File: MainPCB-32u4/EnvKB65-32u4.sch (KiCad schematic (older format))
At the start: 174 parts, among them U1 ATmega32U4-MU, X1 7050 8MHz 5V

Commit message: changed my mind, I wanted the 32u version to have more switches, going to figure out if I can fit the MCU somewhere on the back of the board.
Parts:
- removed C2: 15pf 0402, Capacitor_SMD:C_0402_1005Metric, symbol Device:C
- removed C7: 0.1uF 0402, Capacitor_SMD:C_0402_1005Metric, symbol Device:C
- removed X1: 7050 8MHz 5V, Oscillator:Oscillator_SMD_SeikoEpson_SG8002CA-4Pin_7.0x5.0mm, symbol Oscillator:SG-7050CAN
- added C2, C7: 20pF 0402, Capacitor_SMD:C_0402_1005Metric, symbol Device:C_Small
- added D_131, D_132, D_271, D_272: Diode SOD-323, Diode_SMD:D_SOD-323_HandSoldering, symbol Device:D_Small
- added K_131, K_132, K_271, K_272: KEYSW, MX_Only:MXOnly-1U-NoLED, symbol MX_Alps_Hybrid:MX-NoLED
- added Y1: 8MHz 5032_2P, Crystal:Crystal_SMD_5032-2Pin_5.0x3.2mm, symbol Device:Crystal
- H0, H1, H2, H3, H4, H5: symbol Mechanical:MountingHole -> Mechanical:MountingHole_Pad
- e1: footprint HRO-TYPE-C31-M-12:HRO-TYPE-C-31-M-12 -> HRO-TYPE-C31-M-12:HRO-TYPE-C-31-M-12-Assembly
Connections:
- net GND: now also H0.1, H1.1, H2.1, H3.1, H4.1, H5.1, C2.1, C7.1
- net XTAL1: now also C2.2, Y1.1
- net XTAL2: now also C7.2, Y1.2
- net col0: no longer U1.10 (PB2)
- net col1: no longer U1.11 (PB3)
- net col10: no longer U1.41 (PF0)
- net col11: no longer U1.1 (PE6)
- net col12: no longer U1.8 (PB0)
- net col13: no longer U1.9 (PB1)
- net col14: no longer U1.20 (PD2)
- net col15: now also K_131.1 (COL), K_271.1 (COL); no longer U1.21 (PD3)
- net col16: now also K_132.1 (COL), K_272.1 (COL); no longer U1.22 (PD5)
- net col2: no longer U1.12 (PB7)
- net col3: no longer U1.18 (PD0)
- net col4: no longer U1.19 (PD1)
- net col5: no longer U1.36 (PF7)
- net col6: no longer U1.37 (PF6)
- net col7: no longer U1.38 (PF5)
- net col8: no longer U1.39 (PF4)
- net col9: no longer U1.40 (PF1)
- net row0: now also D_131.1 (K), D_132.1 (K)
- net row1: now also D_271.1 (K), D_272.1 (K)
- new net: D_272.2 (A), K_272.2 (ROW)
- new net: D_271.2 (A), K_271.2 (ROW)
- new net: D_131.2 (A), K_131.2 (ROW)
- new net: D_132.2 (A), K_132.2 (ROW)

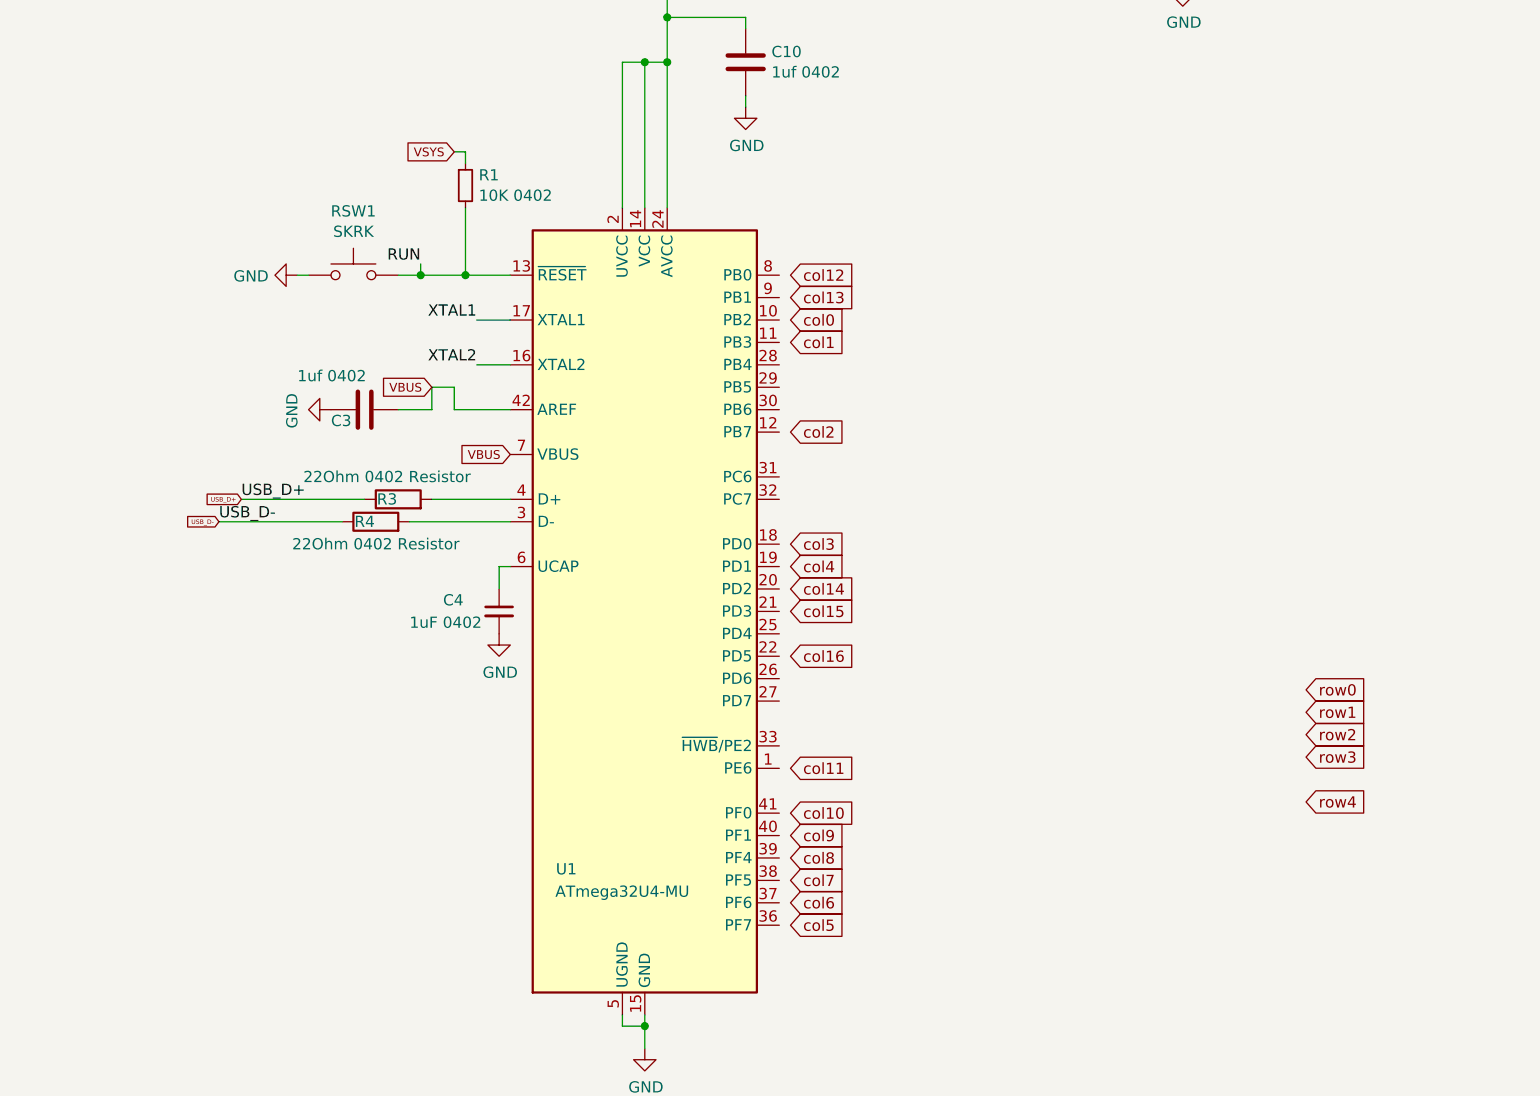
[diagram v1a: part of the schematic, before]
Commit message: finished running traces, probably need to clean up some bits and pieces.
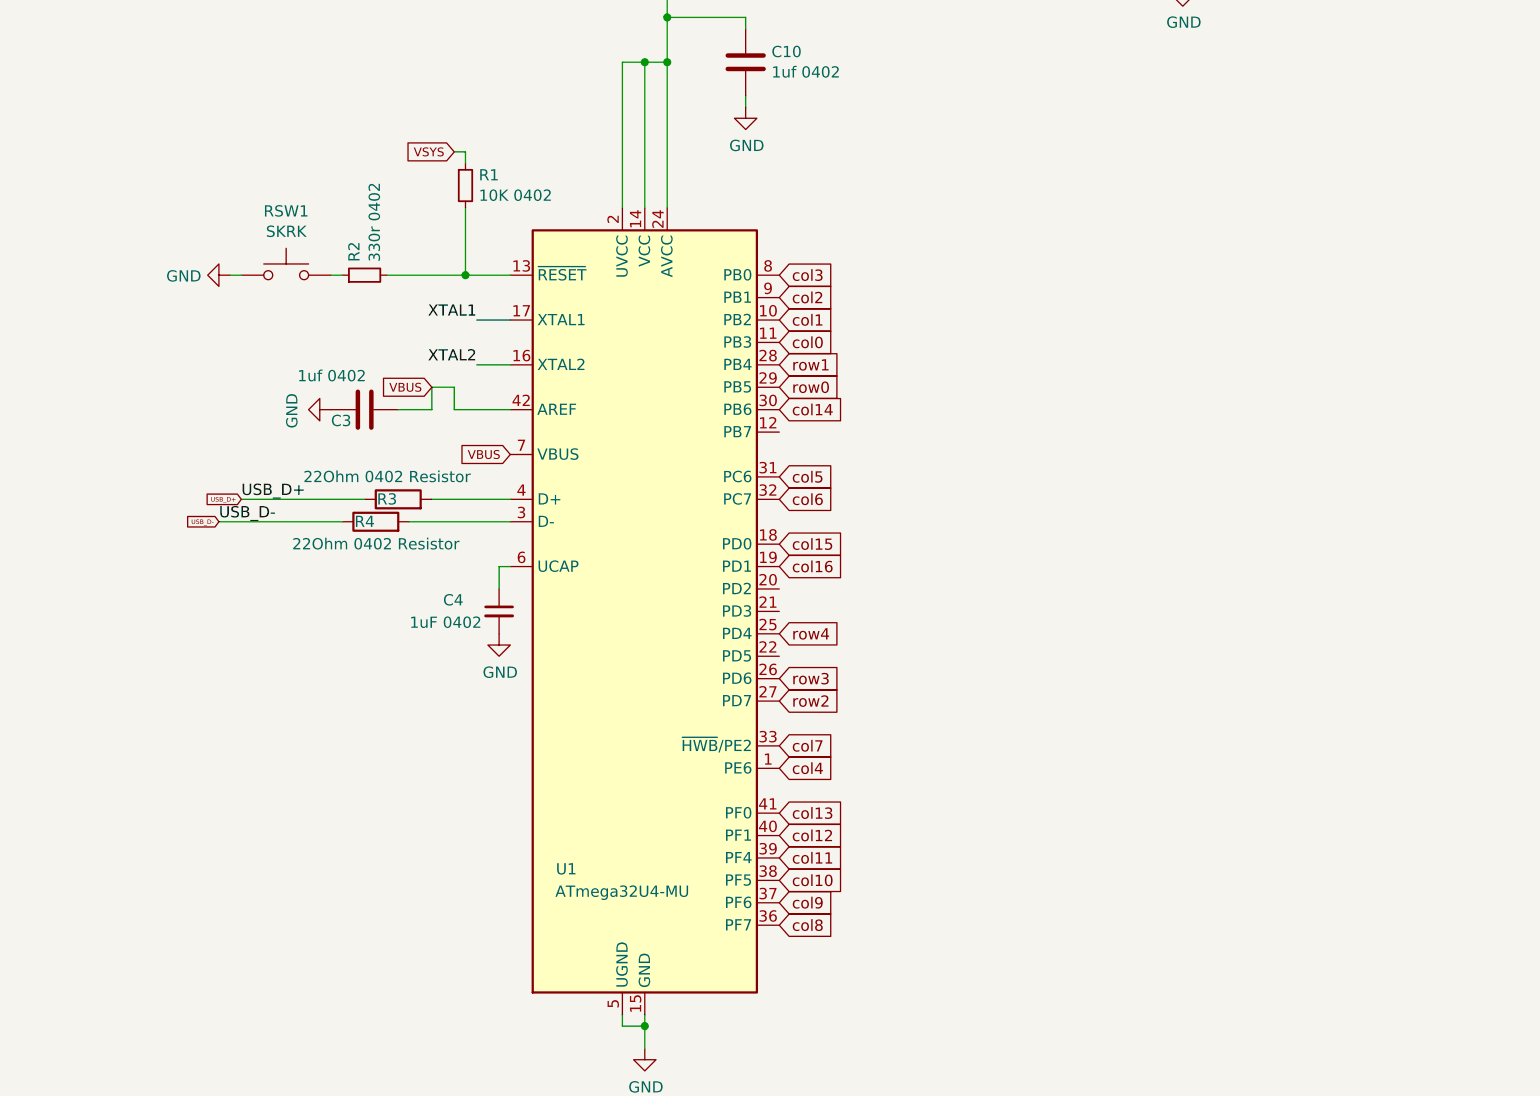
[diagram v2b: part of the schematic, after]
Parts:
- added R2: 330r 0402, Resistor_SMD:R_0402_1005Metric, symbol Device:R_Small
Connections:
- net col0: now also U1.11 (PB3)
- net col1: now also U1.10 (PB2)
- net col10: now also U1.38 (PF5)
- net col11: now also U1.39 (PF4)
- net col12: now also U1.40 (PF1)
- net col13: now also U1.41 (PF0)
- net col14: now also U1.30 (PB6)
- net col15: now also U1.18 (PD0)
- net col16: now also U1.19 (PD1)
- net col2: now also U1.9 (PB1)
- net col3: now also U1.8 (PB0)
- net col4: now also U1.1 (PE6)
- net col5: now also U1.31 (PC6)
- net col6: now also U1.32 (PC7)
- net col7: now also U1.33 (~HWB~/PE2)
- net col8: now also U1.36 (PF7)
- net col9: now also U1.37 (PF6)
- net row0: now also U1.29 (PB5)
- net row1: now also U1.28 (PB4)
- net row2: now also U1.27 (PD7)
- net row3: now also U1.26 (PD6)
- net row4: now also U1.25 (PD4)
- net RUN: no longer names the net of R1.2, U1.13 (~RESET)
- net RUN: now also R2.2; no longer RSW1.2
- new net: R2.1, RSW1.2
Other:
- moved on the sheet: RSW1
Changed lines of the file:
@@
 Wire Wire Line
 	16050 10750 16050 11750
-Text GLabel 6700 3100 2    50   Input ~ 0
+Text GLabel 6650 3200 2    50   Input ~ 0
 col0
-Text GLabel 6700 3200 2    50   Input ~ 0
+Text GLabel 6650 3100 2    50   Input ~ 0
 col1
-Text GLabel 6700 3600 2    50   Input ~ 0
+Text GLabel 6650 3000 2    50   Input ~ 0
 col2
-Text GLabel 6700 4100 2    50   Input ~ 0
+Text GLabel 6650 2900 2    50   Input ~ 0
 col3
-Text GLabel 6700 4200 2    50   Input ~ 0
+Text GLabel 6650 5100 2    50   Input ~ 0
 col4
-Text GLabel 6700 5800 2    50   Input ~ 0
+Text GLabel 6650 3800 2    50   Input ~ 0
 col5
-Text GLabel 6700 5700 2    50   Input ~ 0
+Text GLabel 6650 3900 2    50   Input ~ 0
 col6
-Text GLabel 6700 5600 2    50   Input ~ 0
+Text GLabel 6650 5000 2    50   Input ~ 0
 col7
-Text GLabel 6700 5500 2    50   Input ~ 0
+Text GLabel 6650 5800 2    50   Input ~ 0
 col8
-Text GLabel 6700 5400 2    50   Input ~ 0
+Text GLabel 6650 5700 2    50   Input ~ 0
 col9
-Text GLabel 6700 5300 2    50   Input ~ 0
+Text GLabel 6650 5600 2    50   Input ~ 0
 col10
-Text GLabel 6700 5100 2    50   Input ~ 0
+Text GLabel 6650 5500 2    50   Input ~ 0
 col11
-Text GLabel 6700 2900 2    50   Input ~ 0
+Text GLabel 6650 5400 2    50   Input ~ 0
 col12
-Text GLabel 6700 3000 2    50   Input ~ 0
+Text GLabel 6650 5300 2    50   Input ~ 0
 col13
-Text GLabel 6700 4300 2    50   Input ~ 0
+Text GLabel 6650 3500 2    50   Input ~ 0
 col14
-Text GLabel 6700 4400 2    50   Input ~ 0
+Text GLabel 6650 4100 2    50   Input ~ 0
 col15
-Text GLabel 6700 4600 2    50   Input ~ 0
+Text GLabel 6650 4200 2    50   Input ~ 0
 col16
-Text GLabel 9000 5250 2    50   Input ~ 0
+Text GLabel 6650 4500 2    50   Input ~ 0
 row4
-Text GLabel 9000 5050 2    50   Input ~ 0
+Text GLabel 6650 4700 2    50   Input ~ 0
 row3
-Text GLabel 9000 4950 2    50   Input ~ 0
+Text GLabel 6650 4800 2    50   Input ~ 0
 row2
-Text GLabel 9000 4850 2    50   Input ~ 0
+Text GLabel 6650 3300 2    50   Input ~ 0
 row1
-Text GLabel 9000 4750 2    50   Input ~ 0
+Text GLabel 6650 3400 2    50   Input ~ 0
 row0
 $Comp
@@
 L Switch:SW_Push RSW1
 U 1 1 610FBDD2
-P 4750 2900
-F 0 "RSW1" H 4750 3185 50  0000 C CNN
-F 1 "SKRK" H 4750 3094 50  0000 C CNN
-F 2 "Button_Switch_SMD:SW_Push_SPST_NO_Alps_SKRK" H 4750 3100 50  0001 C CNN
-F 3 "~" H 4750 3100 50  0001 C CNN
-	1    4750 2900
+P 4450 2900
+F 0 "RSW1" H 4450 3185 50  0000 C CNN
+F 1 "SKRK" H 4450 3094 50  0000 C CNN
+F 2 "Button_Switch_SMD:SW_Push_SPST_NO_Alps_SKRK" H 4450 3100 50  0001 C CNN
+F 3 "~" H 4450 3100 50  0001 C CNN
+	1    4450 2900
 	1    0    0    -1
 $EndComp
@@
 L power:GND #PWR01
 U 1 1 610FC4BB
-P 4500 2900
-F 0 "#PWR01" H 4500 2650 50  0001 C CNN
-F 1 "GND" V 4505 2772 50  0000 R CNN
-F 2 "" H 4500 2900 50  0001 C CNN
-F 3 "" H 4500 2900 50  0001 C CNN
-	1    4500 2900
+P 4200 2900
+F 0 "#PWR01" H 4200 2650 50  0001 C CNN
+F 1 "GND" V 4205 2772 50  0000 R CNN
+F 2 "" H 4200 2900 50  0001 C CNN
+F 3 "" H 4200 2900 50  0001 C CNN
+	1    4200 2900
 	0    1    1    0
 $EndComp
 Wire Wire Line
-	4500 2900 4550 2900
+	4200 2900 4250 2900
 Wire Wire Line
 	5250 2600 5250 2900
 Connection ~ 5250 2900
 Wire Wire Line
-	5250 2900 5050 2900
-Wire Wire Line
 	5200 2350 5250 2350
 Wire Wire Line
 	5250 2350 5250 2400
-Text Label 5050 2850 2    50   ~ 0
-RUN
-Wire Wire Line
-	5050 2900 5050 2850
-Connection ~ 5050 2900
-Wire Wire Line
-	5050 2900 4950 2900
 Wire Wire Line
 	6050 1000 6150 1000
@@
 	1    0    0    -1
 $EndComp
+$Comp
+L Device:R_Small R2
+U 1 1 6120126F
+P 4800 2900
+F 0 "R2" H 4859 2946 50  0000 L CNN
+F 1 "330r 0402" H 4859 2855 50  0000 L CNN
+F 2 "Resistor_SMD:R_0402_1005Metric" H 4800 2900 50  0001 C CNN
+F 3 "~" H 4800 2900 50  0001 C CNN
+	1    4800 2900
+	0    -1   -1   0
+$EndComp
+Wire Wire Line
+	4700 2900 4650 2900
+Wire Wire Line
+	4900 2900 5250 2900
 $EndSCHEMATC
